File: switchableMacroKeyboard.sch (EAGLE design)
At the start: 25 parts

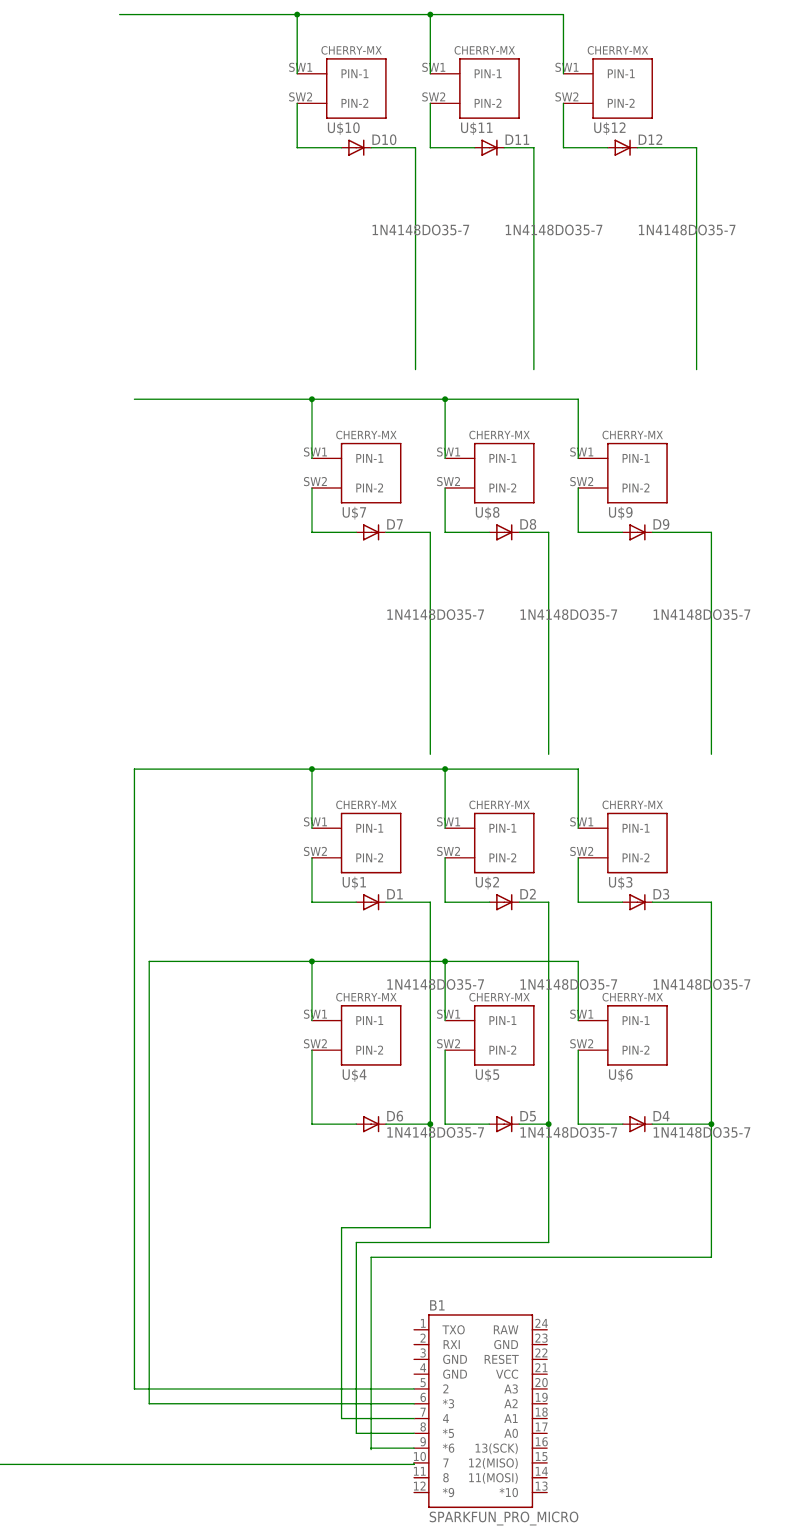
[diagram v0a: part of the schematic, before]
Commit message: Added some pseudo code to source. Connected the switches to the Pro Micro
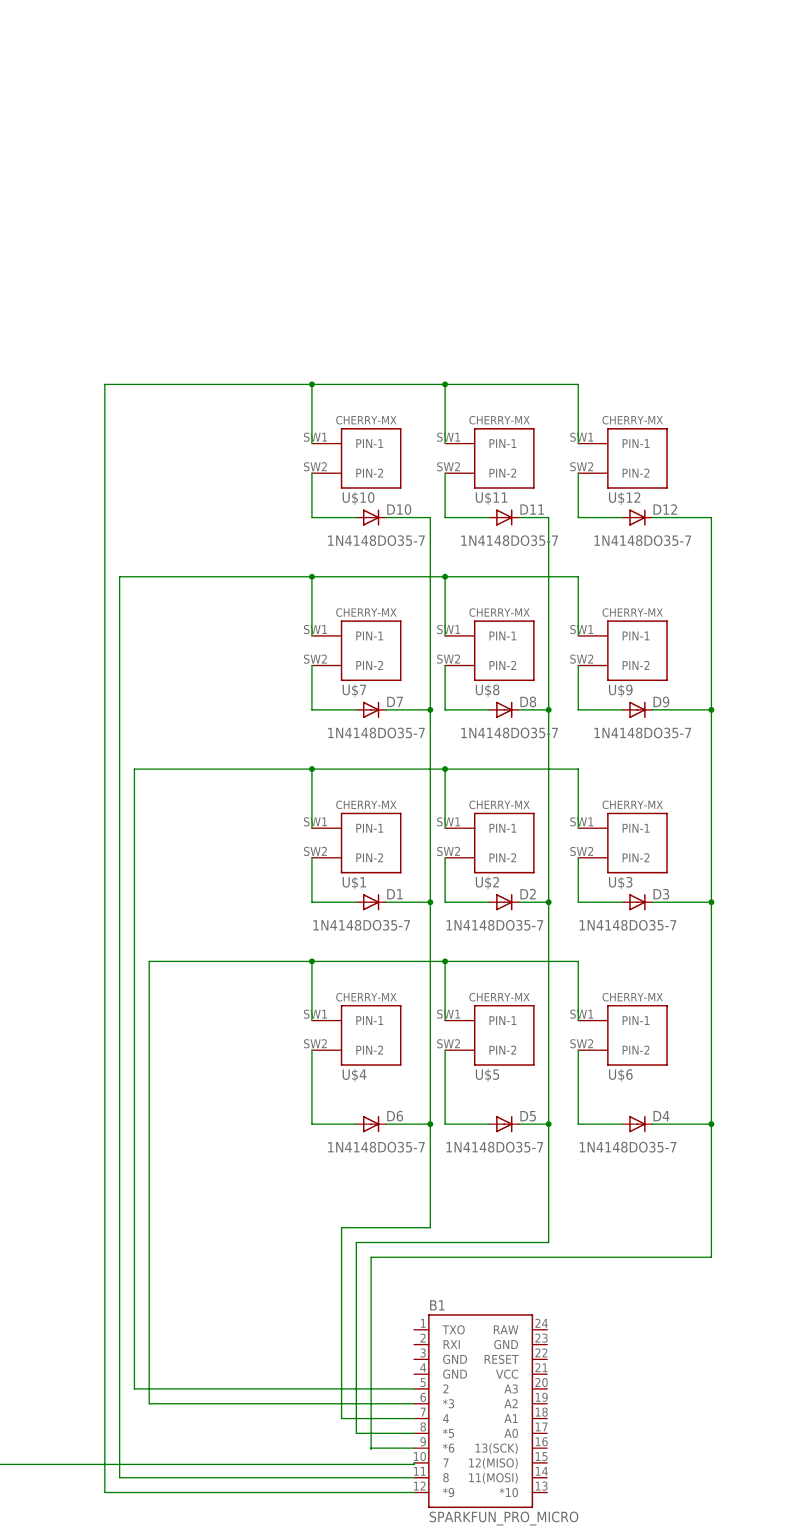
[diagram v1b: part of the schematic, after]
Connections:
- removed net N$10: B1.*5, D2.C, D5.C
- removed net N$11: B1.*6, D3.C, D4.C
- removed net N$21: D7.C
- removed net N$23: D9.C
- removed net N$29: D11.C
- removed net N$9: B1.4, D1.C, D6.C
- net N$17: now also B1.8
- net N$22: now also B1.*5, D11.C, D2.C, D5.C
- net N$24: now also B1.*9
- net N$28: now also B1.4, D1.C, D6.C, D7.C
- net N$30: now also B1.*6, D3.C, D4.C, D9.C
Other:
- moved on the sheet: D10, D11, D12, D7, D8, D9, U$10, U$11, U$12, U$7, U$8, U$9

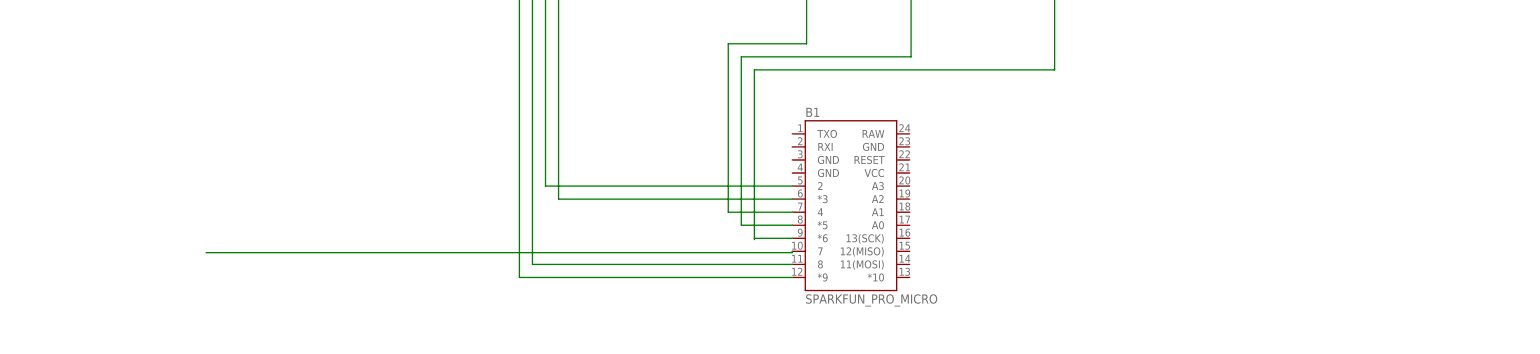
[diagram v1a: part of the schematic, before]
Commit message: Made rotary encoder footprint and symbol. Wired rotary encoder to Pro Micro. Added LCD breakout points. To do: replace switches with tactile switches, add an enable pin (2-pin jumper), and route.
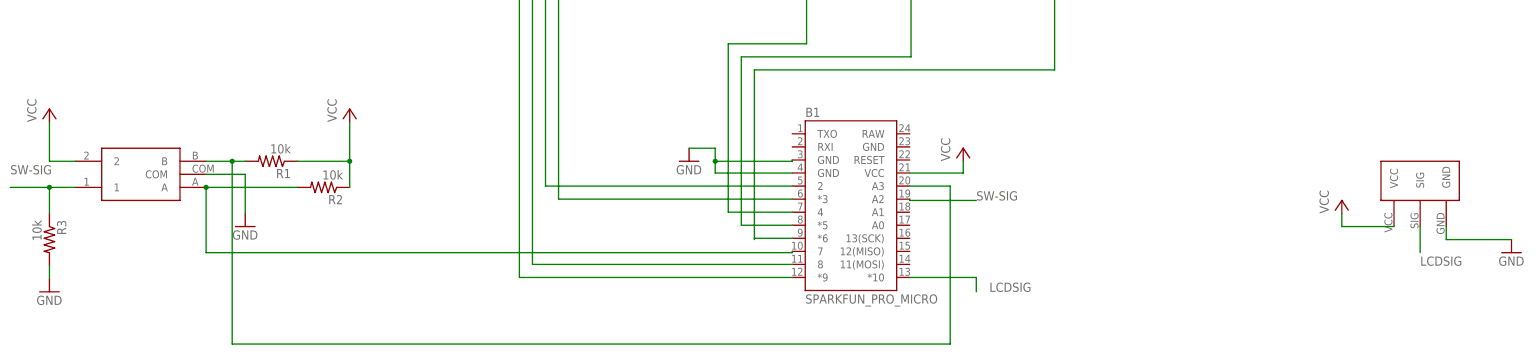
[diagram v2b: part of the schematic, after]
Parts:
- added R1, R2, R3: 10k, rcl:R-US_0207/10
- added U$13: RE-PEC11R-4315F-S0012, ARNEInput:RE-PEC11R-4315F-S0012
- added U$14: 100MIL3PINSIGNAL, switchableMacroKeyboard:100MIL3PINSIGNAL
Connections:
- new net GND: B1.GND, B1.GND@1, R3.2, U$13.COM, U$14.GND
- new net LCDSIG: B1.*10, U$14.SIG
- new net N$9: B1.A3, R1.2, U$13.B
- new net SW-SIG: B1.A2, R3.1, U$13.1
- new net VCC: B1.VCC, R1.1, R2.1, U$13.2, U$14.VCC
- net N$12: now also R2.2, U$13.A
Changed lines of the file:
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@@
 <part name="D11" library="diode" library_urn="urn:adsk.eagle:library:210" deviceset="1N4148" device="DO35-7" package3d_urn="urn:adsk.eagle:package:43339/1"/>
 <part name="D12" library="diode" library_urn="urn:adsk.eagle:library:210" deviceset="1N4148" device="DO35-7" package3d_urn="urn:adsk.eagle:package:43339/1"/>
+<part name="U$13" library="ARNEInput" deviceset="RE-PEC11R-4315F-S0012" device=""/>
+<part name="P+1" library="supply1" library_urn="urn:adsk.eagle:library:371" deviceset="VCC" device=""/>
+<part name="GND1" library="supply1" library_urn="urn:adsk.eagle:library:371" deviceset="GND" device=""/>
+<part name="GND2" library="supply1" library_urn="urn:adsk.eagle:library:371" deviceset="GND" device=""/>
+<part name="R1" library="rcl" library_urn="urn:adsk.eagle:library:334" deviceset="R-US_" device="0207/10" package3d_urn="urn:adsk.eagle:package:23491/2" value="10k"/>
+<part name="R2" library="rcl" library_urn="urn:adsk.eagle:library:334" deviceset="R-US_" device="0207/10" package3d_urn="urn:adsk.eagle:package:23491/2" value="10k"/>
+<part name="P+2" library="supply1" library_urn="urn:adsk.eagle:library:371" deviceset="VCC" device=""/>
+<part name="P+3" library="supply1" library_urn="urn:adsk.eagle:library:371" deviceset="VCC" device=""/>
+<part name="R3" library="rcl" library_urn="urn:adsk.eagle:library:334" deviceset="R-US_" device="0207/10" package3d_urn="urn:adsk.eagle:package:23491/2" value="10k"/>
+<part name="GND3" library="supply1" library_urn="urn:adsk.eagle:library:371" deviceset="GND" device=""/>
+<part name="U$14" library="switchableMacroKeyboard" deviceset="100MIL3PINSIGNAL" device=""/>
+<part name="P+4" library="supply1" library_urn="urn:adsk.eagle:library:371" deviceset="VCC" device=""/>
+<part name="GND4" library="supply1" library_urn="urn:adsk.eagle:library:371" deviceset="GND" device=""/>
 </parts>
 <sheets>
@@
 <attribute name="NAME" x="60.96" y="127.4826" size="1.778" layer="95"/>
 <attribute name="VALUE" x="50.8" y="122.1486" size="1.778" layer="96"/>
+</instance>
+<instance part="U$13" gate="G$1" x="-109.22" y="-20.32" smashed="yes" rot="R90"/>
+<instance part="P+1" gate="VCC" x="-66.04" y="-7.62" smashed="yes">
+<attribute name="VALUE" x="-68.58" y="-10.16" size="1.778" layer="96" rot="R90"/>
+</instance>
+<instance part="GND1" gate="1" x="-86.36" y="-30.48" smashed="yes">
+<attribute name="VALUE" x="-88.9" y="-33.02" size="1.778" layer="96"/>
+</instance>
+<instance part="GND2" gate="1" x="0" y="-17.78" smashed="yes">
+<attribute name="VALUE" x="-2.54" y="-20.32" size="1.778" layer="96"/>
+</instance>
+<instance part="R1" gate="G$1" x="-81.28" y="-17.78" smashed="yes" rot="R180">
+<attribute name="NAME" x="-77.47" y="-19.2786" size="1.778" layer="95" rot="R180"/>
+<attribute name="VALUE" x="-77.47" y="-14.478" size="1.778" layer="96" rot="R180"/>
+</instance>
+<instance part="R2" gate="G$1" x="-71.12" y="-22.86" smashed="yes" rot="R180">
+<attribute name="NAME" x="-67.31" y="-24.3586" size="1.778" layer="95" rot="R180"/>
+<attribute name="VALUE" x="-67.31" y="-19.558" size="1.778" layer="96" rot="R180"/>
+</instance>
+<instance part="P+2" gate="VCC" x="53.34" y="-15.24" smashed="yes">
+<attribute name="VALUE" x="50.8" y="-17.78" size="1.778" layer="96" rot="R90"/>
+</instance>
+<instance part="P+3" gate="VCC" x="-124.46" y="-7.62" smashed="yes">
+<attribute name="VALUE" x="-127" y="-10.16" size="1.778" layer="96" rot="R90"/>
+</instance>
+<instance part="R3" gate="G$1" x="-124.46" y="-33.02" smashed="yes" rot="R270">
+<attribute name="NAME" x="-122.9614" y="-29.21" size="1.778" layer="95" rot="R270"/>
+<attribute name="VALUE" x="-127.762" y="-29.21" size="1.778" layer="96" rot="R270"/>
+</instance>
+<instance part="GND3" gate="1" x="-124.46" y="-43.18" smashed="yes">
+<attribute name="VALUE" x="-127" y="-45.72" size="1.778" layer="96"/>
+</instance>
+<instance part="U$14" gate="G$1" x="142.24" y="-25.4" smashed="yes"/>
+<instance part="P+4" gate="VCC" x="127" y="-25.4" smashed="yes">
+<attribute name="VALUE" x="124.46" y="-27.94" size="1.778" layer="96" rot="R90"/>
+</instance>
+<instance part="GND4" gate="1" x="160.02" y="-35.56" smashed="yes">
+<attribute name="VALUE" x="157.48" y="-38.1" size="1.778" layer="96"/>
 </instance>
 </instances>
@@
 <wire x1="20.066" y1="-35.306" x2="20.066" y2="-35.56" width="0.1524" layer="91"/>
 <wire x1="20.066" y1="-35.56" x2="-93.98" y2="-35.56" width="0.1524" layer="91"/>
+<pinref part="R2" gate="G$1" pin="2"/>
+<pinref part="U$13" gate="G$1" pin="A"/>
+<wire x1="-76.2" y1="-22.86" x2="-93.98" y2="-22.86" width="0.1524" layer="91"/>
+<wire x1="-93.98" y1="-35.56" x2="-93.98" y2="-22.86" width="0.1524" layer="91"/>
+<junction x="-93.98" y="-22.86"/>
+</segment>
+</net>
+<net name="VCC" class="0">
+<segment>
+<pinref part="P+1" gate="VCC" pin="VCC"/>
+<pinref part="R1" gate="G$1" pin="1"/>
+<wire x1="-66.04" y1="-10.16" x2="-66.04" y2="-17.78" width="0.1524" layer="91"/>
+<wire x1="-66.04" y1="-17.78" x2="-76.2" y2="-17.78" width="0.1524" layer="91"/>
+<pinref part="R2" gate="G$1" pin="1"/>
+<wire x1="-66.04" y1="-17.78" x2="-66.04" y2="-22.86" width="0.1524" layer="91"/>
+<junction x="-66.04" y="-17.78"/>
+</segment>
+<segment>
+<pinref part="B1" gate="G$1" pin="VCC"/>
+<pinref part="P+2" gate="VCC" pin="VCC"/>
+<wire x1="42.926" y1="-20.066" x2="53.34" y2="-20.066" width="0.1524" layer="91"/>
+<wire x1="53.34" y1="-20.066" x2="53.34" y2="-17.78" width="0.1524" layer="91"/>
+</segment>
+<segment>
+<pinref part="P+3" gate="VCC" pin="VCC"/>
+<wire x1="-124.46" y1="-10.16" x2="-124.46" y2="-17.78" width="0.1524" layer="91"/>
+<pinref part="U$13" gate="G$1" pin="2"/>
+<wire x1="-124.46" y1="-17.78" x2="-119.38" y2="-17.78" width="0.1524" layer="91"/>
+</segment>
+<segment>
+<pinref part="U$14" gate="G$1" pin="VCC"/>
+<wire x1="137.16" y1="-30.48" x2="127" y2="-30.48" width="0.1524" layer="91"/>
+<pinref part="P+4" gate="VCC" pin="VCC"/>
+<wire x1="127" y1="-30.48" x2="127" y2="-27.94" width="0.1524" layer="91"/>
+</segment>
+</net>
+<net name="N$9" class="0">
+<segment>
+<pinref part="R1" gate="G$1" pin="2"/>
+<pinref part="U$13" gate="G$1" pin="B"/>
+<wire x1="-86.36" y1="-17.78" x2="-88.9" y2="-17.78" width="0.1524" layer="91"/>
+<pinref part="B1" gate="G$1" pin="A3"/>
+<wire x1="-88.9" y1="-17.78" x2="-93.98" y2="-17.78" width="0.1524" layer="91"/>
+<wire x1="42.926" y1="-22.606" x2="50.8" y2="-22.606" width="0.1524" layer="91"/>
+<wire x1="50.8" y1="-22.606" x2="50.8" y2="-53.34" width="0.1524" layer="91"/>
+<wire x1="50.8" y1="-53.34" x2="-88.9" y2="-53.34" width="0.1524" layer="91"/>
+<wire x1="-88.9" y1="-53.34" x2="-88.9" y2="-17.78" width="0.1524" layer="91"/>
+<junction x="-88.9" y="-17.78"/>
+</segment>
+</net>
+<net name="GND" class="0">
+<segment>
+<pinref part="U$13" gate="G$1" pin="COM"/>
+<wire x1="-93.98" y1="-20.32" x2="-86.36" y2="-20.32" width="0.1524" layer="91"/>
+<pinref part="GND1" gate="1" pin="GND"/>
+<wire x1="-86.36" y1="-20.32" x2="-86.36" y2="-27.94" width="0.1524" layer="91"/>
+</segment>
+<segment>
+<pinref part="B1" gate="G$1" pin="GND"/>
+<wire x1="20.066" y1="-20.066" x2="5.08" y2="-20.066" width="0.1524" layer="91"/>
+<wire x1="5.08" y1="-20.066" x2="5.08" y2="-17.78" width="0.1524" layer="91"/>
+<pinref part="GND2" gate="1" pin="GND"/>
+<wire x1="5.08" y1="-17.78" x2="5.08" y2="-15.24" width="0.1524" layer="91"/>
+<wire x1="5.08" y1="-15.24" x2="0" y2="-15.24" width="0.1524" layer="91"/>
+<pinref part="B1" gate="G$1" pin="GND@1"/>
+<wire x1="20.066" y1="-17.526" x2="20.066" y2="-17.78" width="0.1524" layer="91"/>
+<wire x1="20.066" y1="-17.78" x2="5.08" y2="-17.78" width="0.1524" layer="91"/>
+<junction x="5.08" y="-17.78"/>
+</segment>
+<segment>
+<pinref part="R3" gate="G$1" pin="2"/>
+<pinref part="GND3" gate="1" pin="GND"/>
+<wire x1="-124.46" y1="-38.1" x2="-124.46" y2="-40.64" width="0.1524" layer="91"/>
+</segment>
+<segment>
+<pinref part="U$14" gate="G$1" pin="GND"/>
+<pinref part="GND4" gate="1" pin="GND"/>
+<wire x1="147.32" y1="-30.48" x2="147.32" y2="-33.02" width="0.1524" layer="91"/>
+<wire x1="147.32" y1="-33.02" x2="160.02" y2="-33.02" width="0.1524" layer="91"/>
+</segment>
+</net>
+<net name="SW-SIG" class="0">
+<segment>
+<pinref part="U$13" gate="G$1" pin="1"/>
+<wire x1="-119.38" y1="-22.86" x2="-124.46" y2="-22.86" width="0.1524" layer="91"/>
+<pinref part="R3" gate="G$1" pin="1"/>
+<wire x1="-124.46" y1="-22.86" x2="-124.46" y2="-27.94" width="0.1524" layer="91"/>
+<wire x1="-124.46" y1="-22.86" x2="-132.08" y2="-22.86" width="0.1524" layer="91"/>
+<junction x="-124.46" y="-22.86"/>
+<label x="-132.08" y="-20.32" size="1.778" layer="95"/>
+</segment>
+<segment>
+<pinref part="B1" gate="G$1" pin="A2"/>
+<wire x1="42.926" y1="-25.146" x2="42.926" y2="-25.4" width="0.1524" layer="91"/>
+<wire x1="42.926" y1="-25.4" x2="55.88" y2="-25.4" width="0.1524" layer="91"/>
+<label x="55.88" y="-25.4" size="1.778" layer="95"/>
+</segment>
+</net>
+<net name="LCDSIG" class="0">
+<segment>
+<pinref part="B1" gate="G$1" pin="*10"/>
+<wire x1="42.926" y1="-40.386" x2="55.88" y2="-40.386" width="0.1524" layer="91"/>
+<wire x1="55.88" y1="-40.386" x2="55.88" y2="-43.18" width="0.1524" layer="91"/>
+<label x="58.42" y="-43.18" size="1.778" layer="95"/>
+</segment>
+<segment>
+<pinref part="U$14" gate="G$1" pin="SIG"/>
+<wire x1="142.24" y1="-30.48" x2="142.24" y2="-35.56" width="0.1524" layer="91"/>
+<label x="142.24" y="-38.1" size="1.778" layer="95"/>
 </segment>
 </net>
@@
 packages will not be understood (or retained) with this version.
 </note>
+<note version="8.4" severity="warning">
+Since Version 8.4, EAGLE supports properties for SPICE simulation.
+Probes in schematics and SPICE mapping objects found in parts and library devices
+will not be understood with this version. Update EAGLE to the latest version
+for full support of SPICE simulation.
+</note>
 </compatibility>
